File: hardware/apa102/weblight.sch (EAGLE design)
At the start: 16 parts, among them U1 ATtiny85-20SU

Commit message: a-mf1
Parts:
- removed JP-USB-TOP: USBPCB, SparkFun-Connectors:USBPCB
- removed R5: 470, rcl:R-US_R0402
- added HOLE1, HOLE2, HOLE3, HOLE4: MOUNTINGHOLE2.0, microbuilder:MOUNTINGHOLE2.0
- C1: value 10uF -> 1uF
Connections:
- removed net DIN_RAW: R5.2, U1.PB0(MOSI)
- net DIN_1: now also U1.PB0(MOSI); no longer R5.1
- net GND: now also C1.1, C2.1; no longer C1.2, C2.2, JP-USB-TOP.GND
- net USB_D_MINUS: now also R2.2; no longer R3.2
- net USB_D_MINUS_RAW: now also R1.2, R2.1; no longer JP-USB-TOP.D-, R1.1, R3.1
- net USB_D_PLUS: now also R3.1; no longer R2.2
- net USB_D_PLUS_RAW: now also R3.2; no longer JP-USB-TOP.D+, R2.1
- net VCC: now also C1.2, C2.2, R1.1; no longer C1.1, C2.1, JP-USB-TOP.VBUS, R1.2
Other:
- moved on the sheet: C1, C2, JP-USB-MICRO, R1, R2, R3, R4, U1

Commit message: Forgot ICSP
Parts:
- added ICSP: POGOPIN-CONNONEHOLE, Protofusion:POGOPIN-CONNONEHOLE
- JP-USB-MICRO: value (none) -> USB
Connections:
- removed net CLK_1: LED1.CI, U1.PB2(SCK/ADC1)
- removed net DIN_1: LED1.DI, U1.PB0(MOSI)
- new net CLK_1/SCK: ICSP.SCK, LED1.CI, U1.PB2(SCK/ADC1)
- new net DIN_1/MOSI: ICSP.MOSI, LED1.DI, U1.PB0(MOSI)
- new net MISO: ICSP.MISO, U1.PB1(MISO)
- net GND: now also ICSP.GND
- net N_RESET: now also ICSP.\RST
- net USB_D_MINUS: now also R3.2; no longer R2.2
- net USB_D_MINUS_RAW: now also R3.1; no longer R2.1
- net USB_D_PLUS: now also R2.1; no longer R3.1
- net USB_D_PLUS_RAW: now also R2.2; no longer R3.2
- net VCC: now also ICSP.VCC
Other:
- moved on the sheet: JP-USB-MICRO, R1, R2, R3, R4

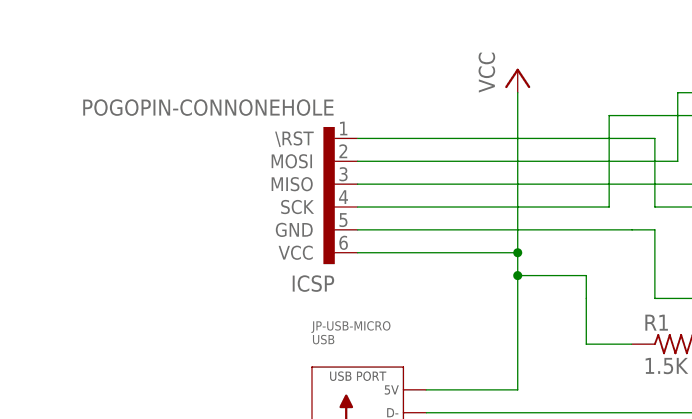
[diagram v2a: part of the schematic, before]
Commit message: Substitute 6-pin pogo layout
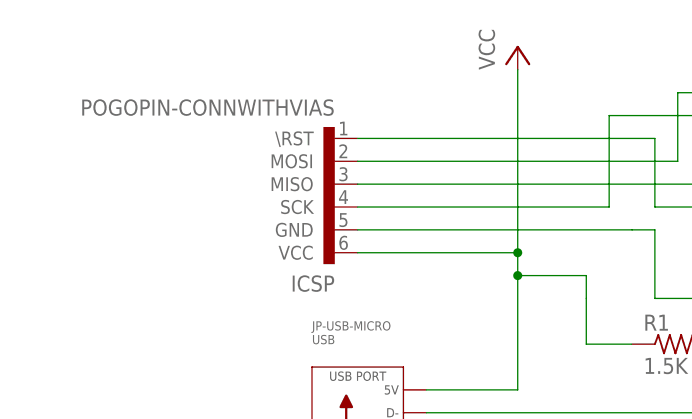
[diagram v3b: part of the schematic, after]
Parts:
- ICSP: value POGOPIN-CONNONEHOLE -> POGOPIN-CONNWITHVIAS; device Protofusion:POGOPIN-CONNONEHOLE -> weblight:POGOPIN-CONNWITHVIAS
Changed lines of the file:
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@@
 <part name="HOLE4" library="microbuilder" deviceset="MOUNTINGHOLE" device="2.0"/>
 <part name="HOLE1" library="microbuilder" deviceset="MOUNTINGHOLE" device="2.0"/>
-<part name="ICSP" library="Protofusion" deviceset="POGOPIN-CONN" device="ONEHOLE"/>
+<part name="ICSP" library="weblight" deviceset="POGOPIN-CONN" device="WITHVIAS" value="POGOPIN-CONNWITHVIAS"/>
 </parts>
 <sheets>
@@
 <instance part="U1" gate="G$1" x="-2.54" y="73.66"/>
 <instance part="JP-USB-MICRO" gate="G$1" x="-73.66" y="53.34"/>
-<instance part="P+2" gate="VCC" x="-55.88" y="93.98"/>
+<instance part="P+2" gate="VCC" x="-55.88" y="96.52"/>
 <instance part="GND2" gate="1" x="-20.32" y="30.48"/>
 <instance part="GND3" gate="1" x="-33.02" y="30.48"/>
@@
 <wire x1="-55.88" y1="58.42" x2="-66.04" y2="58.42" width="0.1524" layer="91"/>
 <wire x1="-55.88" y1="71.12" x2="-55.88" y2="73.66" width="0.1524" layer="91"/>
-<wire x1="-55.88" y1="73.66" x2="-55.88" y2="91.44" width="0.1524" layer="91"/>
+<wire x1="-55.88" y1="73.66" x2="-55.88" y2="93.98" width="0.1524" layer="91"/>
 <wire x1="-43.18" y1="63.5" x2="-48.26" y2="63.5" width="0.1524" layer="91"/>
 <wire x1="-48.26" y1="63.5" x2="-48.26" y2="68.58" width="0.1524" layer="91"/>
